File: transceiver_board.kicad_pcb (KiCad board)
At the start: 2 copper layers, 212.5 x 77.2 mm, 134 parts, among them J1 85505-5113, J2 Conn_01x01_Male, J3 Laser, J4 Conn_01x01_Male, J5 Receiver Connector, Q1 BC547, Q2 BC547, T1 S558-5999-46-F, U1 LAN83C185-JT, U2 ltc6752ims8-2-pbf, U4 AP63203WU, U5 AP63205WU, U6 LM317_TO-220, U7 LM317_TO-220, Y1 25 MHz

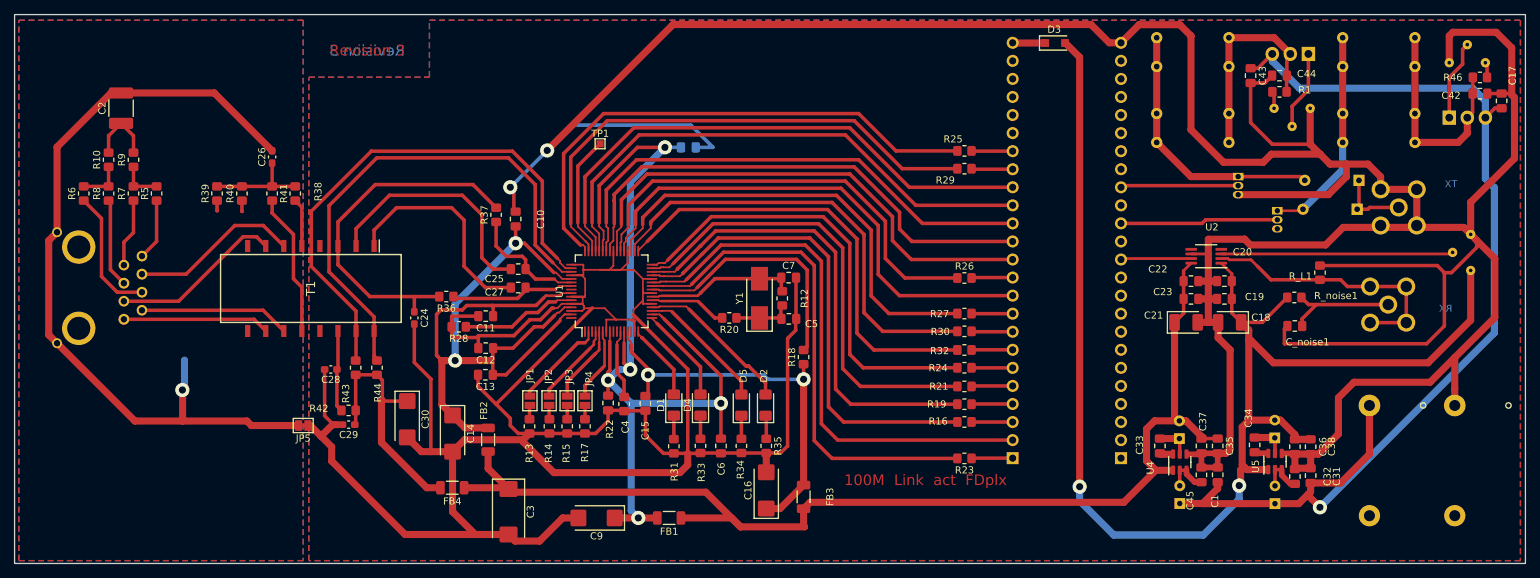
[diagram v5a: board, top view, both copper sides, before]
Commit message: fixed ethernet fp, moved 12v via and embiggened small track
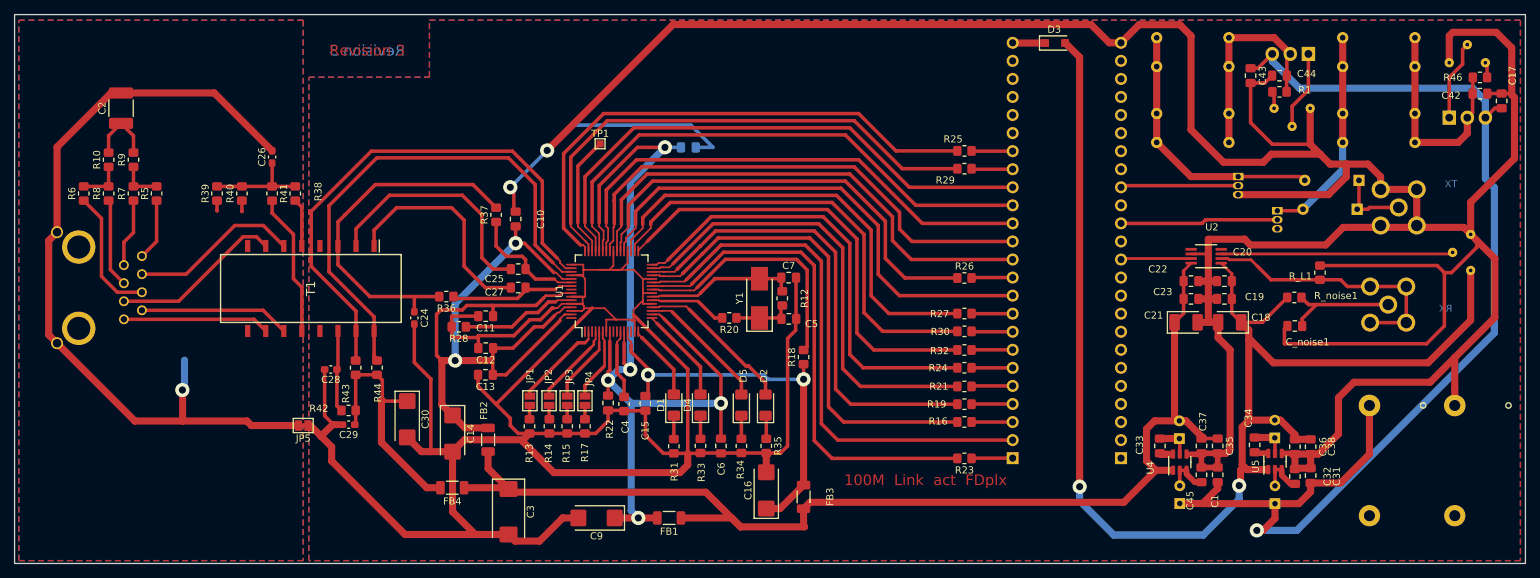
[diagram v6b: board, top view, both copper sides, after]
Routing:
- net +12V: track 151.4 -> 164.4 mm
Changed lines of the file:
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@@
     (property "Value_1" "85505-5113")
     (attr through_hole)
-    (fp_text reference "J1" (at -0.085 15.225 90) (layer "B.SilkS")
+    (fp_text reference "J1" (at -0.085 15.225 270) (layer "B.SilkS")
       (effects (font (size 1.27 1.27) (thickness 0.254)) (justify mirror))
     )
-    (fp_text value "85505-5113" (at -0.26877 10.78492 90) (layer "B.SilkS") hide
+    (fp_text value "85505-5113" (at -0.26877 10.78492 270) (layer "B.SilkS") hide
       (effects (font (size 1.27 1.27) (thickness 0.254)) (justify mirror))
     )
-    (fp_text user "${REFERENCE}" (at -0.085 15.225 90) (layer "B.Fab")
+    (fp_text user "${REFERENCE}" (at -0.085 15.225 270) (layer "B.Fab")
       (effects (font (size 1.27 1.27) (thickness 0.254)) (justify mirror))
     )
+    (fp_line (start 8.3 13.57) (end 8.3 0.9) (layer "B.SilkS") (width 0.2))
+    (fp_line (start -8.3 -5.23) (end -8.3 -0.9) (layer "B.SilkS") (width 0.2))
+    (fp_line (start -8.3 -5.23) (end 8.3 -5.23) (layer "B.SilkS") (width 0.2))
+    (fp_line (start -8.3 13.57) (end -8.3 0.9) (layer "B.SilkS") (width 0.2))
+    (fp_line (start 8.3 -5.23) (end 8.3 -0.9) (layer "B.SilkS") (width 0.2))
     (fp_line (start 8.3 13.57) (end -8.3 13.57) (layer "B.SilkS") (width 0.2))
-    (fp_line (start 8.3 13.57) (end 8.3 0.761) (layer "B.SilkS") (width 0.2))
-    (fp_line (start -8.3 -5.23) (end -8.3 -0.761) (layer "B.SilkS") (width 0.2))
-    (fp_line (start 8.3 -5.23) (end 8.3 -0.761) (layer "B.SilkS") (width 0.2))
-    (fp_line (start -8.3 13.57) (end -8.3 0.761) (layer "B.SilkS") (width 0.2))
-    (fp_line (start -8.3 -5.23) (end 8.3 -5.23) (layer "B.SilkS") (width 0.2))
     (fp_circle (center -9.506 9.364) (end -9.506 9.24094) (layer "B.SilkS") (width 0.2) (fill none))
+    (fp_line (start 8.3 -5.23) (end -8.3 -5.23) (layer "B.Fab") (width 0.2))
+    (fp_line (start 8.3 13.57) (end 8.3 -5.23) (layer "B.Fab") (width 0.2))
+    (fp_line (start -8.3 -5.23) (end -8.3 13.57) (layer "B.Fab") (width 0.2))
     (fp_line (start -8.3 13.57) (end 8.3 13.57) (layer "B.Fab") (width 0.2))
-    (fp_line (start -8.3 -5.23) (end -8.3 13.57) (layer "B.Fab") (width 0.2))
-    (fp_line (start 8.3 13.57) (end 8.3 -5.23) (layer "B.Fab") (width 0.2))
-    (fp_line (start 8.3 -5.23) (end -8.3 -5.23) (layer "B.Fab") (width 0.2))
-    (pad "1" thru_hole circle (at -4.445 9.4 90) (size 1.54081 1.54081) (drill 0.9) (layers *.Cu *.Mask)
+    (pad "1" thru_hole circle (at -4.445 9.4 90) (size 1.4 1.4) (drill 0.9) (layers *.Cu *.Mask)
       (net 34 "ETH-TXp") (pinfunction "1") (pintype "passive"))
-    (pad "2" thru_hole circle (at -3.175 11.94 90) (size 1.500298 1.500298) (drill 0.9) (layers *.Cu *.Mask)
+    (pad "2" thru_hole circle (at -3.175 11.94 90) (size 1.4 1.4) (drill 0.9) (layers *.Cu *.Mask)
       (net 35 "ETH-TXn") (pinfunction "2") (pintype "passive"))
-    (pad "3" thru_hole circle (at -1.905 9.4 90) (size 1.51 1.51) (drill 0.9) (layers *.Cu *.Mask)
+    (pad "3" thru_hole circle (at -1.905 9.4 90) (size 1.4 1.4) (drill 0.9) (layers *.Cu *.Mask)
       (net 36 "ETH-RXp") (pinfunction "3") (pintype "passive"))
-    (pad "4" thru_hole circle (at -0.635 11.94 90) (size 1.52 1.52) (drill 0.9) (layers *.Cu *.Mask)
+    (pad "4" thru_hole circle (at -0.635 11.94 90) (size 1.4 1.4) (drill 0.9) (layers *.Cu *.Mask)
       (net 138 "Net-(J1-Pad4)") (pinfunction "4") (pintype "passive"))
-    (pad "5" thru_hole circle (at 0.635 9.4 90) (size 1.530816 1.530816) (drill 0.9) (layers *.Cu *.Mask)
+    (pad "5" thru_hole circle (at 0.635 9.4 90) (size 1.4 1.4) (drill 0.9) (layers *.Cu *.Mask)
       (net 139 "Net-(J1-Pad5)") (pinfunction "5") (pintype "passive"))
-    (pad "6" thru_hole circle (at 1.905 11.94 90) (size 1.540292 1.540292) (drill 0.9) (layers *.Cu *.Mask)
+    (pad "6" thru_hole circle (at 1.905 11.94 90) (size 1.4 1.4) (drill 0.9) (layers *.Cu *.Mask)
       (net 37 "ETH-RXn") (pinfunction "6") (pintype "passive"))
-    (pad "7" thru_hole circle (at 3.175 9.4 90) (size 1.5 1.5) (drill 0.9) (layers *.Cu *.Mask)
+    (pad "7" thru_hole circle (at 3.175 9.4 90) (size 1.4 1.4) (drill 0.9) (layers *.Cu *.Mask)
       (net 140 "Net-(J1-Pad7)") (pinfunction "7") (pintype "passive"))
-    (pad "8" thru_hole circle (at 4.445 11.94 90) (size 1.510296 1.510296) (drill 0.9) (layers *.Cu *.Mask)
+    (pad "8" thru_hole circle (at 4.445 11.94 90) (size 1.4 1.4) (drill 0.9) (layers *.Cu *.Mask)
       (net 141 "Net-(J1-Pad8)") (pinfunction "8") (pintype "passive"))
     (pad "9" thru_hole circle (at -5.715 3.05 90) (size 4.7 4.7) (drill 3.25) (layers *.Cu *.Mask))
     (pad "10" thru_hole circle (at 5.715 3.05 90) (size 4.7 4.7) (drill 3.25) (layers *.Cu *.Mask))
-    (pad "11" thru_hole circle (at -7.805 0 90) (size 1.4 1.4) (drill 0.9) (layers *.Cu *.Mask)
+    (pad "11" thru_hole circle (at -7.805 0 90) (size 1.7 1.7) (drill 1.2) (layers *.Cu *.Mask)
       (net 133 "GND1") (pinfunction "11") (pintype "power_in"))
-    (pad "12" thru_hole circle (at 7.805 0 90) (size 1.4 1.4) (drill 0.9) (layers *.Cu *.Mask)
+    (pad "12" thru_hole circle (at 7.805 0 90) (size 1.7 1.7) (drill 1.2) (layers *.Cu *.Mask)
       (net 133 "GND1") (pinfunction "12") (pintype "power_in"))
     (model "85505-5113.stp"
@@
   (segment (start 180.28325 109.96675) (end 183.49975 109.96675) (width 1) (layer "F.Cu") (net 1))
   (segment (start 224.5855 54.3775) (end 223.266 55.697) (width 0.508) (layer "F.Cu") (net 1))
+  (segment (start 193.675 112.075) (end 193.675 109.9875) (width 1) (layer "F.Cu") (net 1))
   (segment (start 191.2835 48.7465) (end 193.294 46.736) (width 0.508) (layer "F.Cu") (net 1))
   (segment (start 225.552 54.3775) (end 224.5855 54.3775) (width 0.508) (layer "F.Cu") (net 1))
@@
   (segment (start 197.025 109.9875) (end 193.675 109.9875) (width 1) (layer "F.Cu") (net 1))
   (segment (start 198.69 107.0795) (end 198.69 108.3225) (width 1) (layer "F.Cu") (net 1))
-  (segment (start 198.34375 108.84375) (end 200 110.5) (width 1) (layer "F.Cu") (net 1))
   (segment (start 190.246 48.7465) (end 191.2835 48.7465) (width 0.508) (layer "F.Cu") (net 1))
   (segment (start 206.963001 103.036999) (end 206.963001 96.1815) (width 1) (layer "F.Cu") (net 1))
   (segment (start 198.69 108.3225) (end 198.34375 108.66875) (width 1) (layer "F.Cu") (net 1))
-  (segment (start 198.34375 108.66875) (end 198.34375 108.84375) (width 1) (layer "F.Cu") (net 1))
+  (segment (start 191.125 113.75) (end 192 113.75) (width 1) (layer "F.Cu") (net 1))
+  (segment (start 192 113.75) (end 193.675 112.075) (width 1) (layer "F.Cu") (net 1))
   (segment (start 193.675 109.9875) (end 188.8975 109.9875) (width 1) (layer "F.Cu") (net 1))
   (segment (start 183.49975 109.96675) (end 185.61925 107.84725) (width 1) (layer "F.Cu") (net 1))
   (segment (start 188.8975 109.9875) (end 183.5205 109.9875) (width 1) (layer "F.Cu") (net 1))
   (segment (start 202.9205 107.0795) (end 206.963001 103.036999) (width 1) (layer "F.Cu") (net 1))
-  (via (at 200 110.5) (size 2) (drill 1) (layers "F.Cu" "B.Cu") (net 1))
-  (segment (start 193.294 47.752) (end 197.104 51.562) (width 1) (layer "B.Cu") (net 1))
-  (segment (start 224.536 65.532) (end 224.536 85.964) (width 1) (layer "B.Cu") (net 1))
-  (segment (start 224.536 85.964) (end 200 110.5) (width 1) (layer "B.Cu") (net 1))
-  (segment (start 197.104 51.562) (end 221.488 51.562) (width 1) (layer "B.Cu") (net 1))
-  (segment (start 193.294 46.736) (end 193.294 47.752) (width 1) (layer "B.Cu") (net 1))
-  (segment (start 223.266 53.34) (end 223.266 55.118) (width 1) (layer "B.Cu") (net 1))
-  (segment (start 223.266 55.118) (end 223.266 64.262) (width 1) (layer "B.Cu") (net 1))
-  (segment (start 221.488 51.562) (end 223.266 53.34) (width 1) (layer "B.Cu") (net 1))
-  (segment (start 223.266 64.262) (end 224.536 65.532) (width 1) (layer "B.Cu") (net 1))
+  (via (at 191.125 113.75) (size 2) (drill 1) (layers "F.Cu" "B.Cu") (net 1))
+  (segment (start 193.294 47.752) (end 193.294 46.736) (width 1) (layer "B.Cu") (net 1))
+  (segment (start 224.536 65.532) (end 223.266 64.262) (width 1) (layer "B.Cu") (net 1))
+  (segment (start 223.266 64.262) (end 223.266 53.34) (width 1) (layer "B.Cu") (net 1))
+  (segment (start 224.536 85.964) (end 224.536 65.532) (width 1) (layer "B.Cu") (net 1))
+  (segment (start 221.488 51.562) (end 197.104 51.562) (width 1) (layer "B.Cu") (net 1))
+  (segment (start 223.266 53.34) (end 221.488 51.562) (width 1) (layer "B.Cu") (net 1))
+  (segment (start 191.125 113.75) (end 196.75 113.75) (width 1) (layer "B.Cu") (net 1))
+  (segment (start 197.104 51.562) (end 193.294 47.752) (width 1) (layer "B.Cu") (net 1))
+  (segment (start 196.75 113.75) (end 224.536 85.964) (width 1) (layer "B.Cu") (net 1))
   (segment (start 115.7025 102.865) (end 115.625 102.865) (width 0.5) (layer "F.Cu") (net 2))
   (segment (start 86.8 115.25) (end 85.875 114.325) (width 1) (layer "F.Cu") (net 2))
@@
   (segment (start 197.402 68.79) (end 197.612 68.58) (width 0.375) (layer "F.Cu") (net 144))
   (segment (start 203.2 44.45) (end 203.2 59.182) (width 1) (layer "F.Cu") (net 144))
-  (segment (start 194 68.79) (end 197.402 68.79) (width 0.375) (layer "F.Cu") (net 144))
+  (segment (start 194 68.79) (end 197.402 68.79) (width 0.5) (layer "F.Cu") (net 144))
   (segment (start 203.2 59.182) (end 203.2 62.992) (width 1) (layer "B.Cu") (net 144))
   (segment (start 203.2 62.992) (end 197.612 68.58) (width 1) (layer "B.Cu") (net 144))
